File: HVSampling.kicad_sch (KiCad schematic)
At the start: 45 parts, among them K6 SPU01M-05, U6 AMC1351DWV, U7 AMC1351DWV, U8 TLV6002

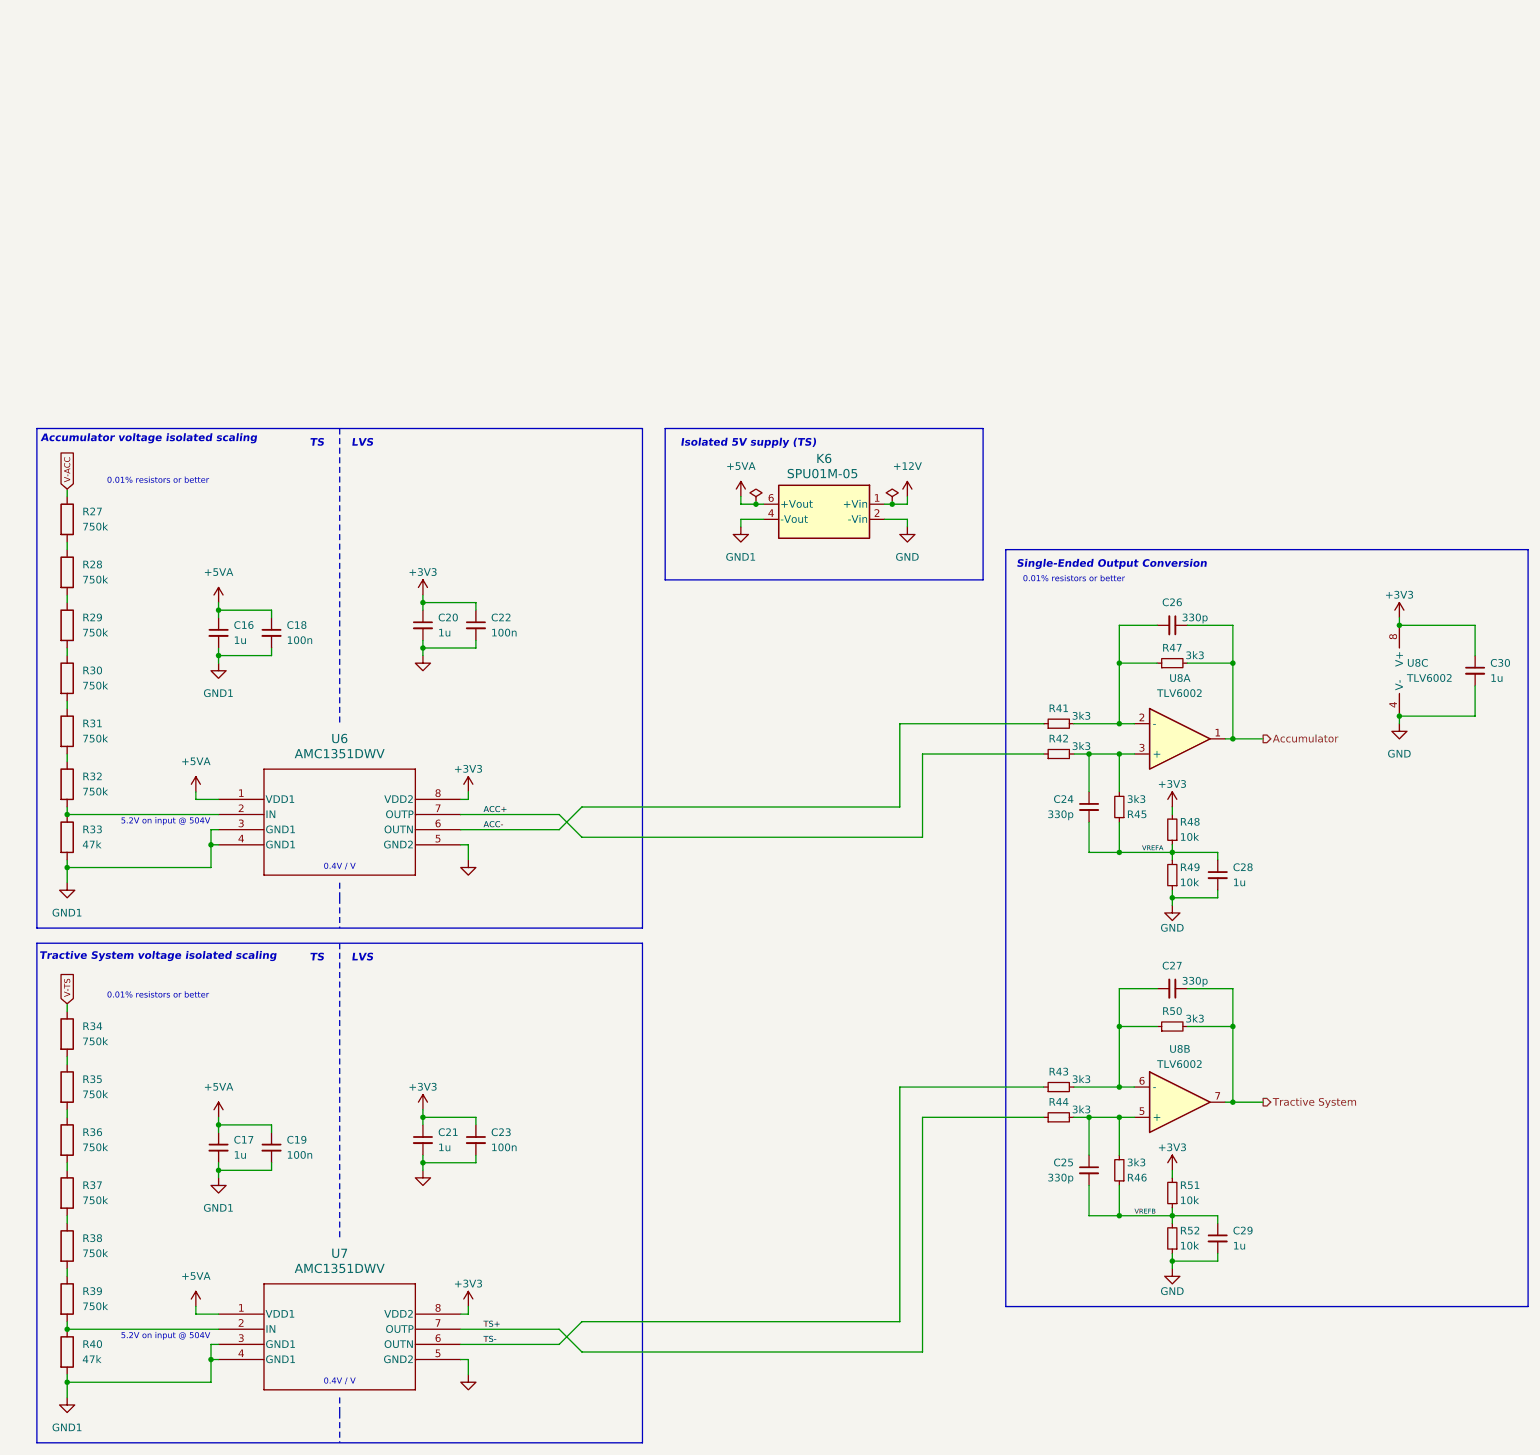
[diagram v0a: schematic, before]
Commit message: Updated to single pole relay, removed relay drivers
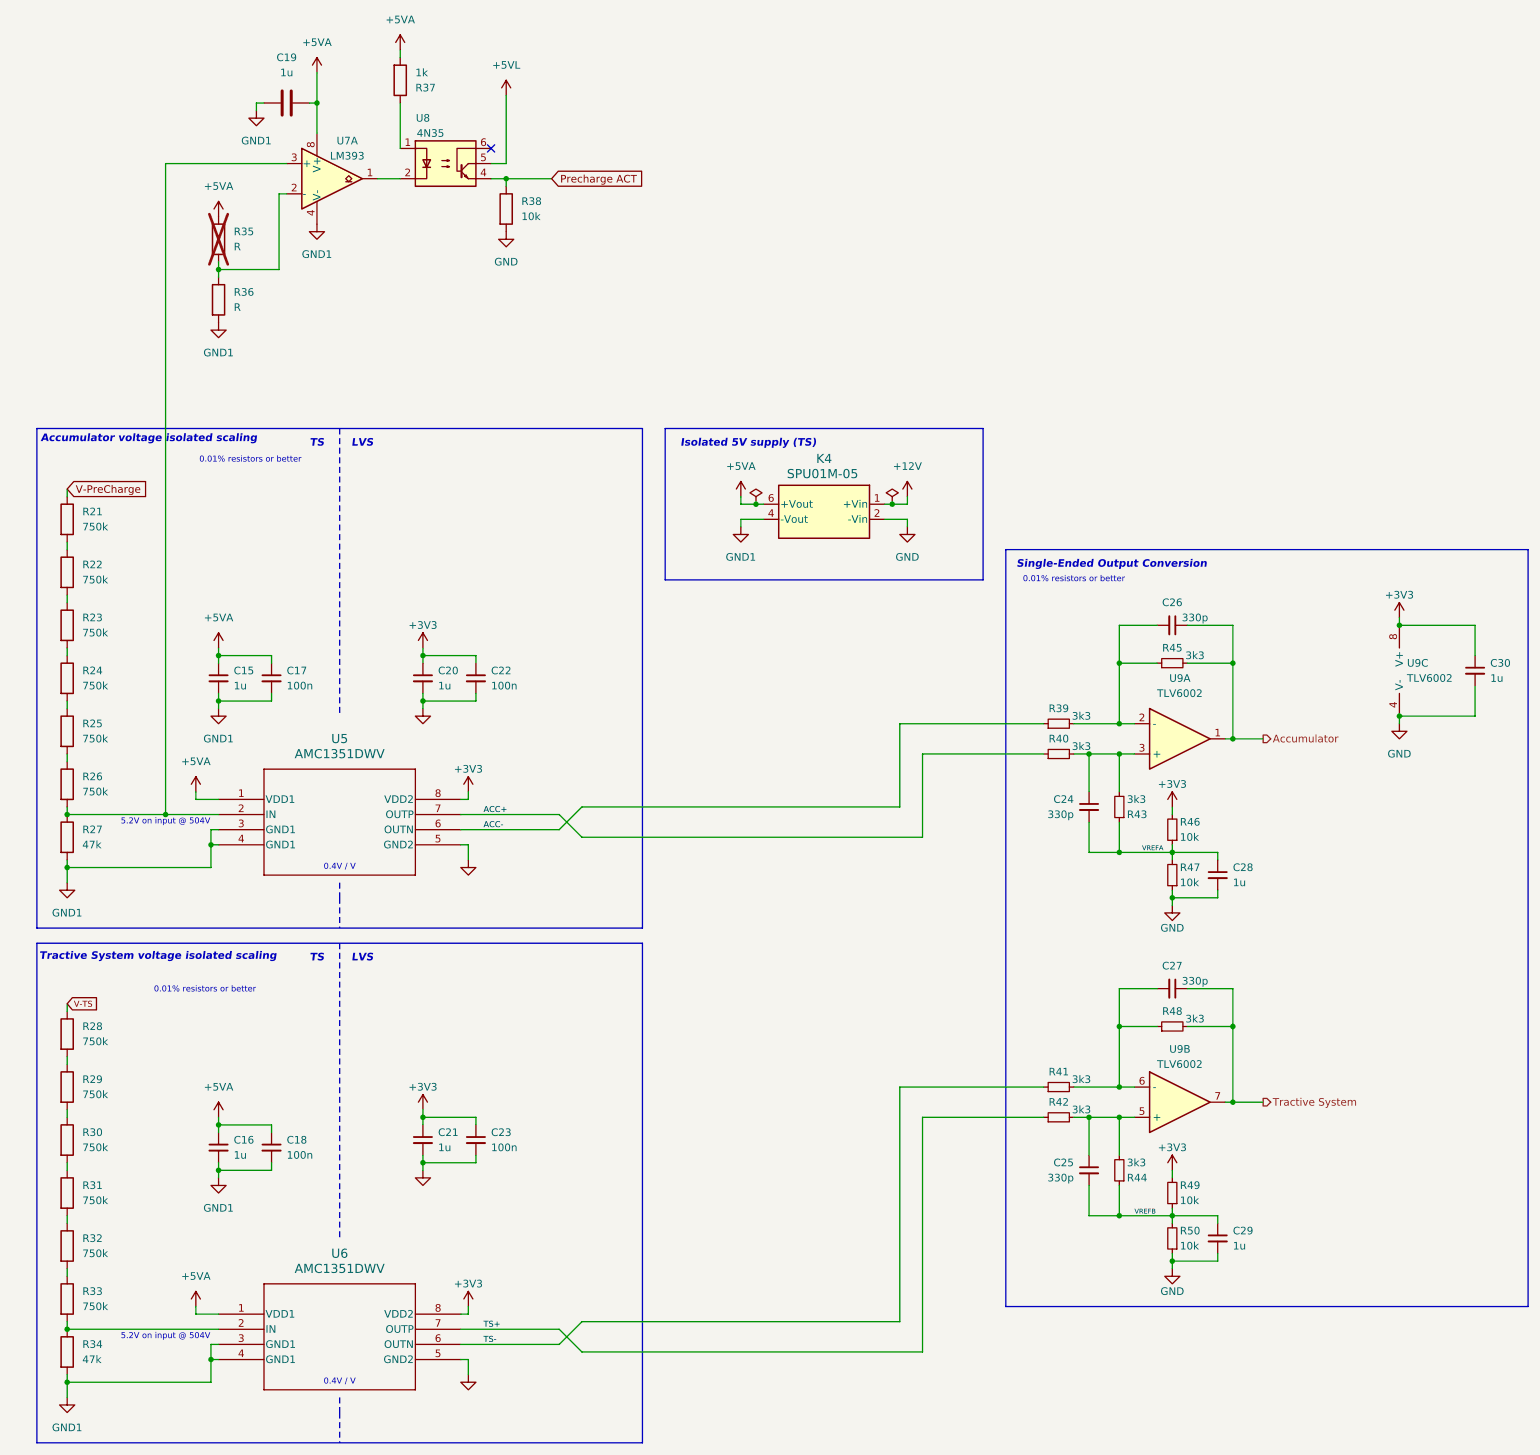
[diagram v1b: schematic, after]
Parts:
- added C19: 1u, Capacitor_SMD:C_0603_1608Metric, symbol Device:C
- added R35, R36: R, Resistor_SMD:R_0603_1608Metric, symbol Device:R
- added R37: 1k, Resistor_SMD:R_0603_1608Metric, symbol Device:R
- added R38: 10k, Resistor_SMD:R_0603_1608Metric, symbol Device:R
- added U7: LM393, Package_SO:SOIC-8_3.9x4.9mm_P1.27mm, symbol Comparator:LM393
- added U8: 4N35, Package_DIP:DIP-6_W7.62mm, symbol Isolator:4N35
- renumbered C16 to C15, C17 to C16, C18 to C17, C19 to C18, K6 to K4, R27 to R21, R28 to R22, R29 to R23, R30 to R24, R31 to R25, R32 to R26, R33 to R27, R34 to R28, R35 to R29, R36 to R30, R37 to R31, R38 to R32, R39 to R33, R40 to R34, R41 to R39, R42 to R40, R43 to R41, R44 to R42, R45 to R43, R46 to R44, R47 to R45, R48 to R46, R49 to R47, R50 to R48, R51 to R49, R52 to R50, U6 to U5, U7 to U6, U8 to U9
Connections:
- net +5VA: now also C19.2, R35.1, R37.2, U7.8 (V+)
- net GND: now also R38.2
- net GND1: now also C19.1, R36.2, U7.4 (V-)
- net at R26.2, R27.1, U5.2 (IN): now also U7.3 (+)
- net V-ACC renamed V-PreCharge
- new net: U7.1, U8.2
- new net: R35.2, R36.1, U7.2 (-)
- new net: R37.1, U8.1
- new net +5VL: U8.5
- new net Precharge ACT: R38.1, U8.4
- no-connect marks 0 -> 1
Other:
- moved on the sheet: C15, C17, C20, C22

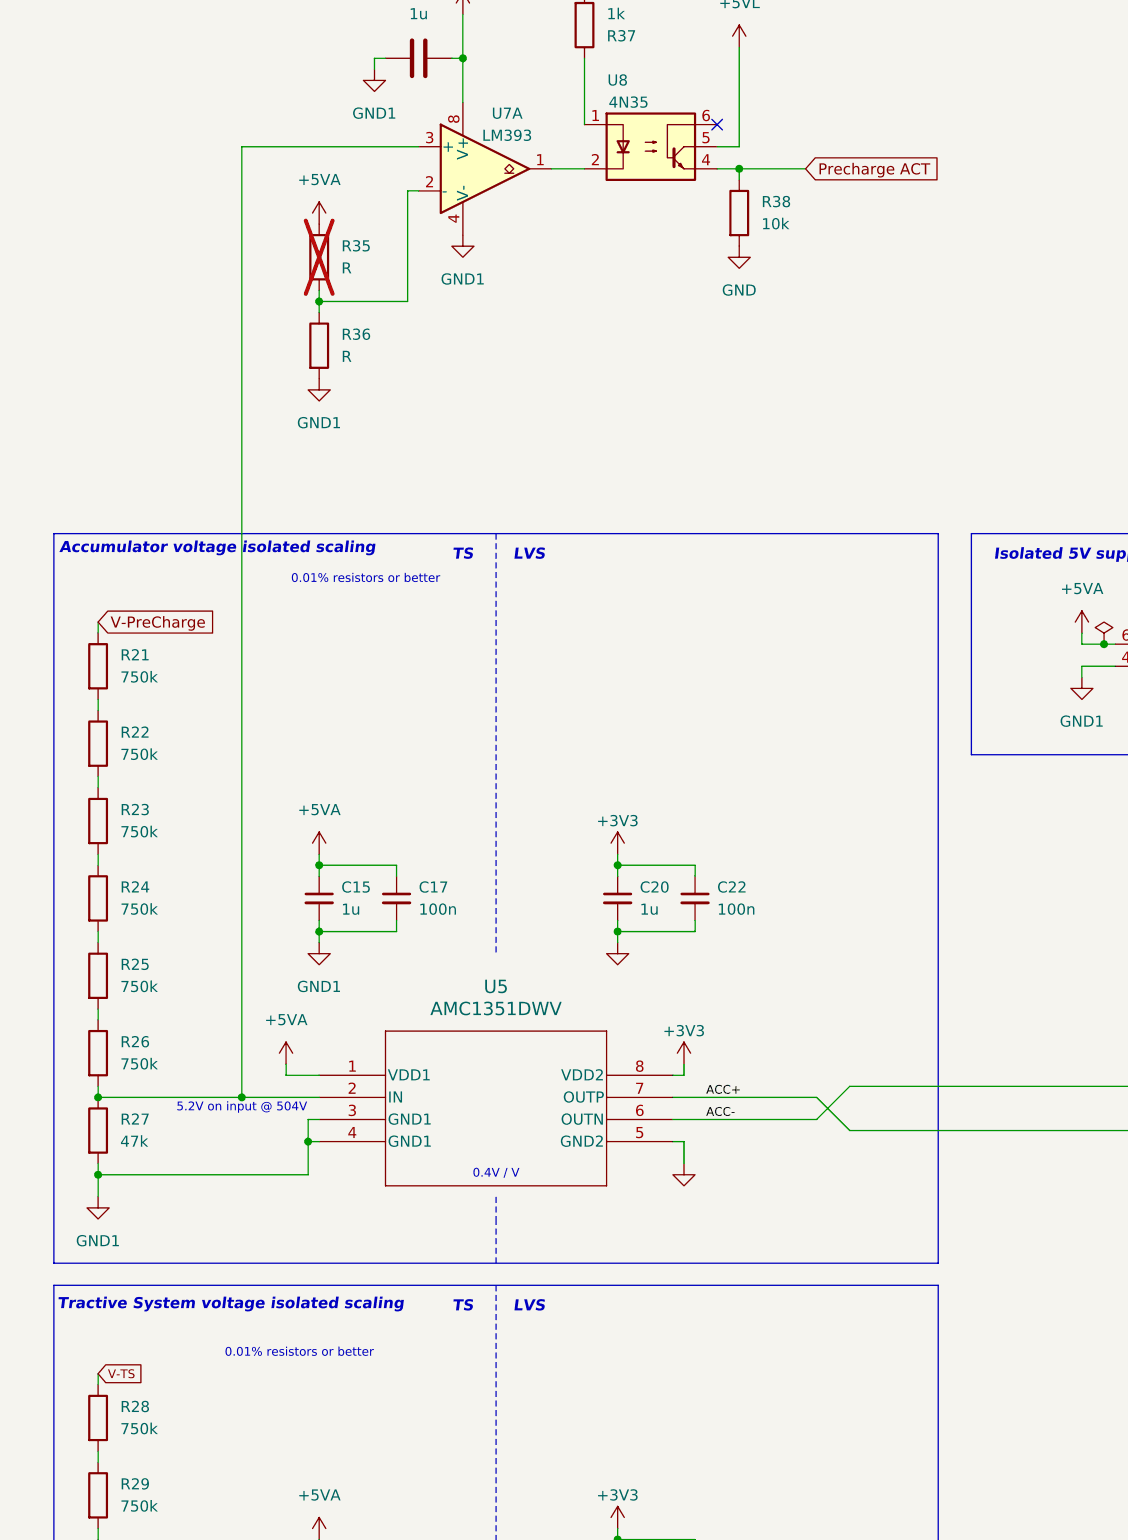
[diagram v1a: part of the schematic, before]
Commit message: schematic: Cleanup all global labels
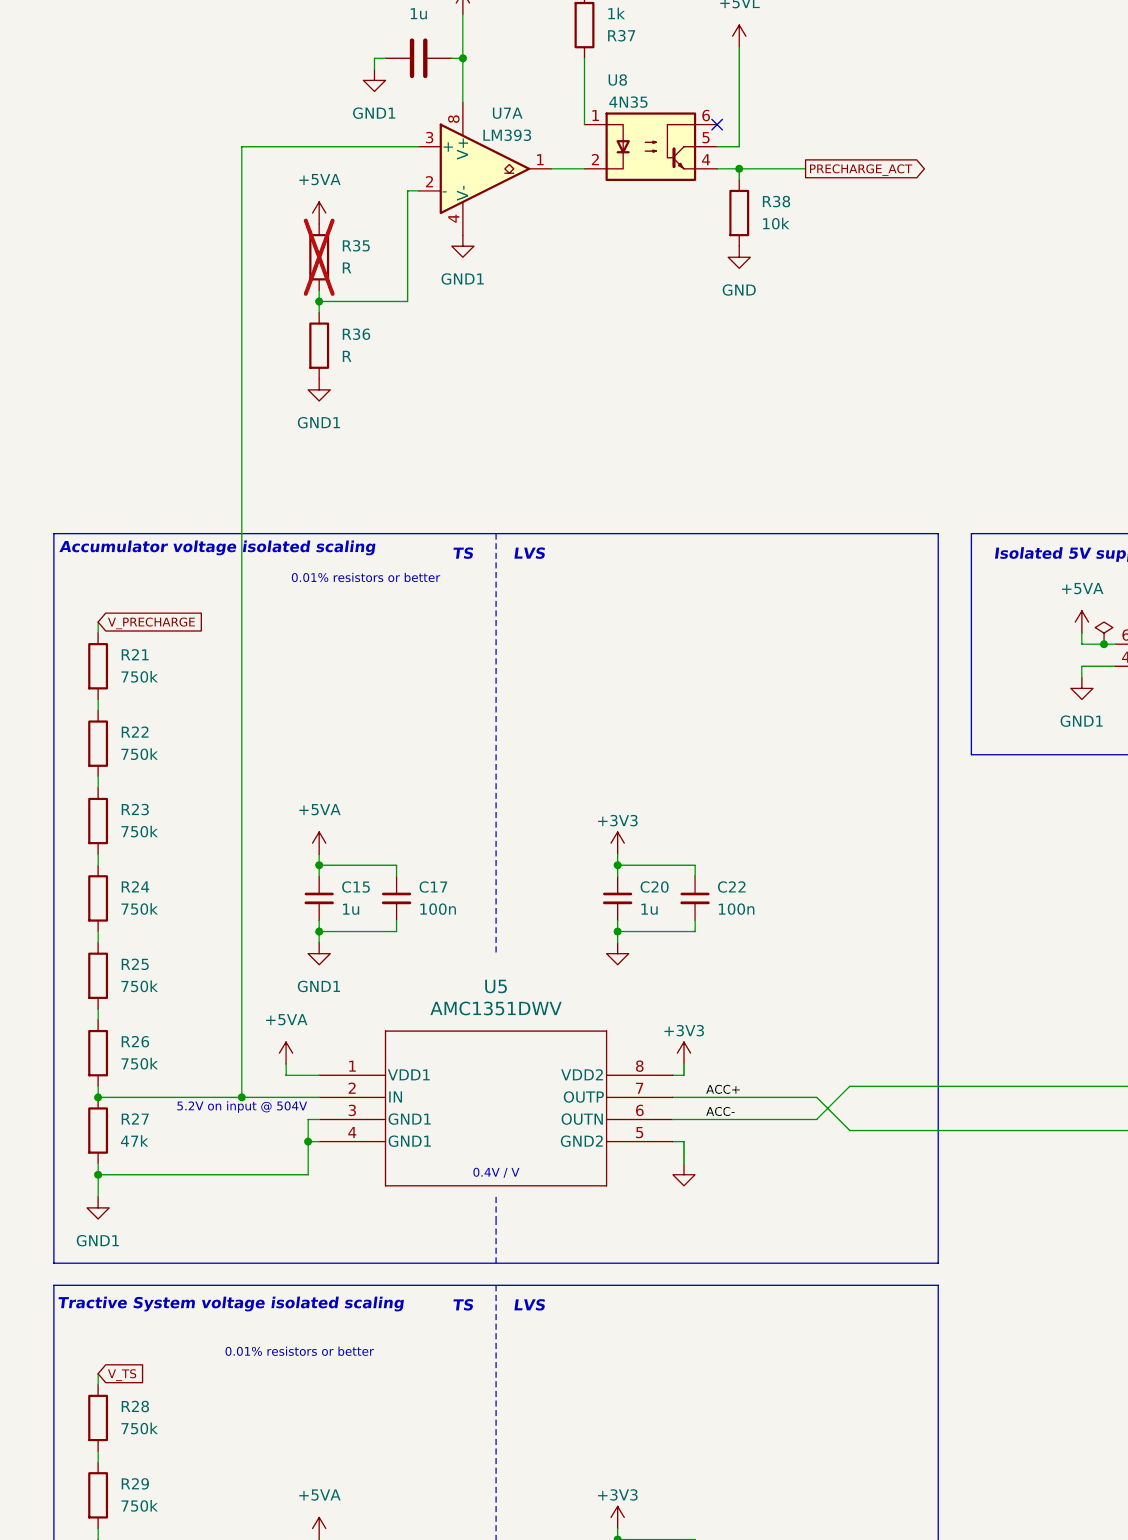
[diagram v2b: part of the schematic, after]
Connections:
- net Precharge ACT renamed PRECHARGE_ACT
- net V-PreCharge renamed V_PRECHARGE
- net V-TS renamed V_TS
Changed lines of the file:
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@@
 		(rev "${REVISION}")
 		(company "York Formula Student")
-		(comment 1 "Designed by Josh B and Logan C")
+		(comment 1 "Designed by Josh B, Logan C, and Owen S")
 	)
 	(rectangle
@@
 		)
 	)
-	(global_label "V-PreCharge"
+	(global_label "V_PRECHARGE"
 		(shape input)
 		(at 20.32 25.4 0)
@@
 		(effects
 			(font
-				(size 1.27 1.27)
+				(size 1 1)
 			)
 			(justify left)
 		)
 		(property "Intersheetrefs" "${INTERSHEET_REFS}"
-			(at 35.7028 25.4 0)
+			(at 33.0036 25.4 0)
 			(effects
 				(font
@@
 		)
 	)
-	(global_label "Precharge ACT"
-		(shape input)
+	(global_label "PRECHARGE_ACT"
+		(shape output)
 		(at 101.6 -26.67 0)
 		(fields_autoplaced yes)
 		(effects
 			(font
-				(size 1.27 1.27)
+				(size 1 1)
 			)
 			(justify left)
 		)
 		(property "Intersheetrefs" "${INTERSHEET_REFS}"
-			(at 118.4342 -26.67 0)
+			(at 116.0455 -26.67 0)
 			(effects
 				(font
@@
 		)
 	)
-	(global_label "V-TS"
+	(global_label "V_TS"
 		(shape input)
 		(at 20.32 111.76 0)
@@
 		)
 		(property "Intersheetrefs" "${INTERSHEET_REFS}"
-			(at 26.4798 111.76 0)
+			(at 26.0036 111.76 0)
 			(effects
 				(font
